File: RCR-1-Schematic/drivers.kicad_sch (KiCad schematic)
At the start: 11 parts, among them T1 Transformer_1P_1S

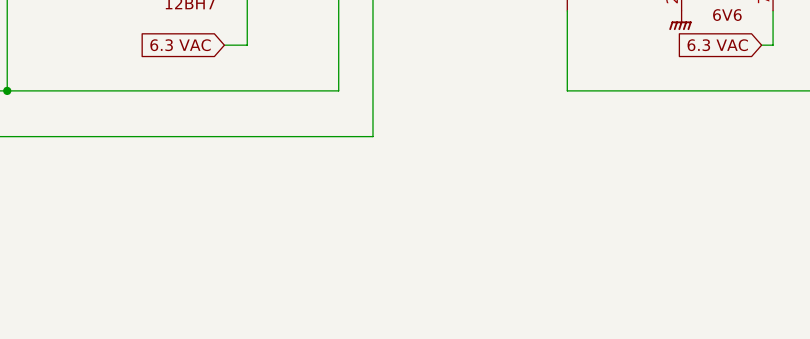
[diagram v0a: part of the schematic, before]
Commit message: Add some oscilloscope screenshots, fixed some mistakes
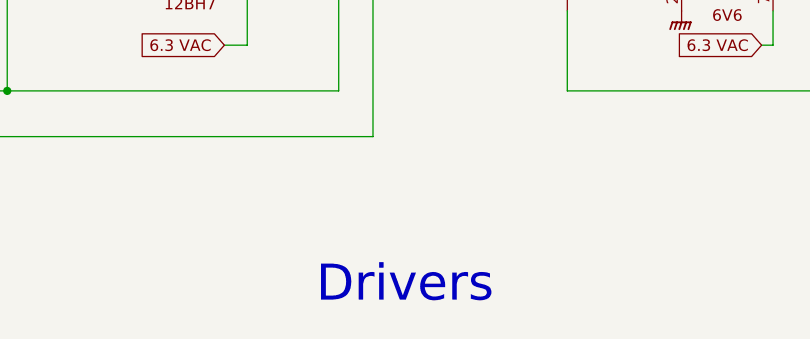
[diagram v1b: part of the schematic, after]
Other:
- note added: "Drivers"
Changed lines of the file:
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@@
+		)
+	)
+	(text "Drivers"
+		(exclude_from_sim no)
+		(at 147.066 137.16 0)
+		(effects
+			(font
+				(size 4 4)
+			)
 		)
 	)
